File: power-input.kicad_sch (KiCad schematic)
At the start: 21 parts, among them J204 Conn_01x02, J301 Conn_01x02, U202 XL1509-3.3

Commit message: Rename Ferrite_Bead to FerriteBead
Symbol name changed between KiCad 5 and 6...
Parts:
- FB301: symbol Device:Ferrite_Bead -> Device:FerriteBead
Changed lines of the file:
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@@
     (pin "2")
   )
-  (symbol (lib_id "Device:Ferrite_Bead") (at 113.03 53.34 270) (unit 1)
+  (symbol (lib_id "Device:FerriteBead") (at 113.03 53.34 270) (unit 1)
     (in_bom yes) (on_board yes)
     (property "Reference" "FB301" (id 0) (at 113.03 46.3804 90))

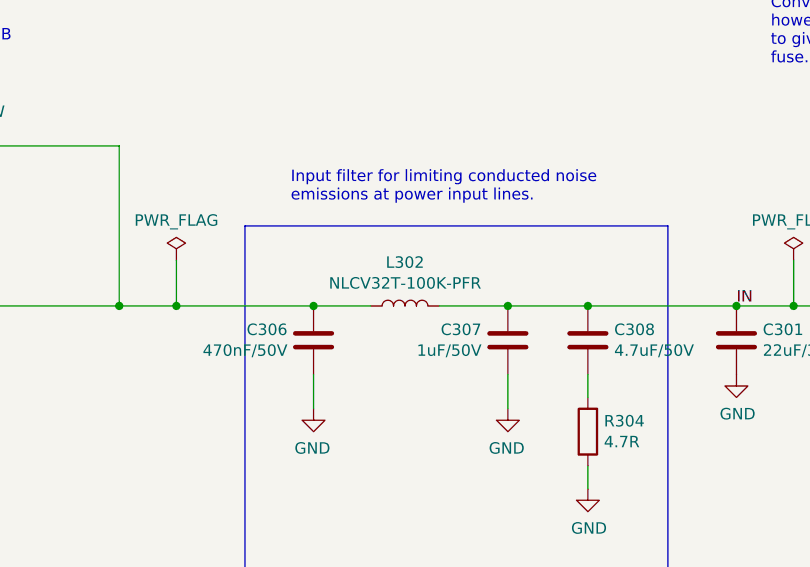
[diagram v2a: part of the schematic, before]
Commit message: One more component swap due to part availability
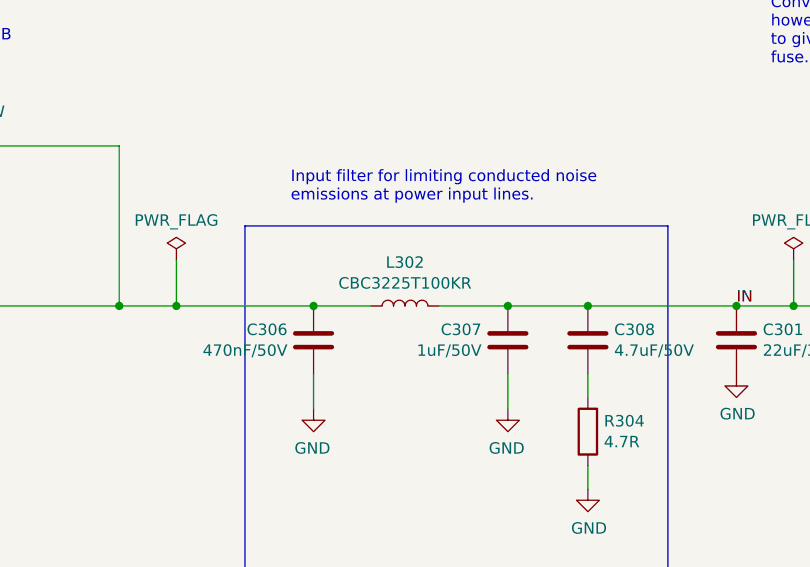
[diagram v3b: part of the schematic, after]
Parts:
- L302: value NLCV32T-100K-PFR -> CBC3225T100KR; LCSC C74563 -> C90321; Notes Alternative: CBC3225T100KR -> Alternatives: CBC3225T100KR, NLCV32T-100K-PFR
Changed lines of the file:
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@@
     (in_bom yes) (on_board yes)
     (property "Reference" "L302" (id 0) (at 121.92 117.094 90))
-    (property "Value" "NLCV32T-100K-PFR" (id 1) (at 121.92 119.4054 90))
+    (property "Value" "CBC3225T100KR" (id 1) (at 121.92 119.4054 90))
     (property "Footprint" "Inductor_SMD:L_1210_3225Metric" (id 2) (at 121.92 121.92 0)
       (effects (font (size 1.27 1.27)) hide)
@@
       (effects (font (size 1.27 1.27)) hide)
     )
-    (property "LCSC" "C74563" (id 6) (at 121.92 121.92 0)
+    (property "LCSC" "C90321" (id 6) (at 121.92 121.92 0)
       (effects (font (size 1.27 1.27)) hide)
     )
-    (property "Notes" "Alternative: CBC3225T100KR" (id 7) (at 121.92 121.92 90)
+    (property "Notes" "Alternatives: CBC3225T100KR, NLCV32T-100K-PFR" (id 7) (at 121.92 121.92 90)
       (effects (font (size 1.27 1.27)) hide)
     )

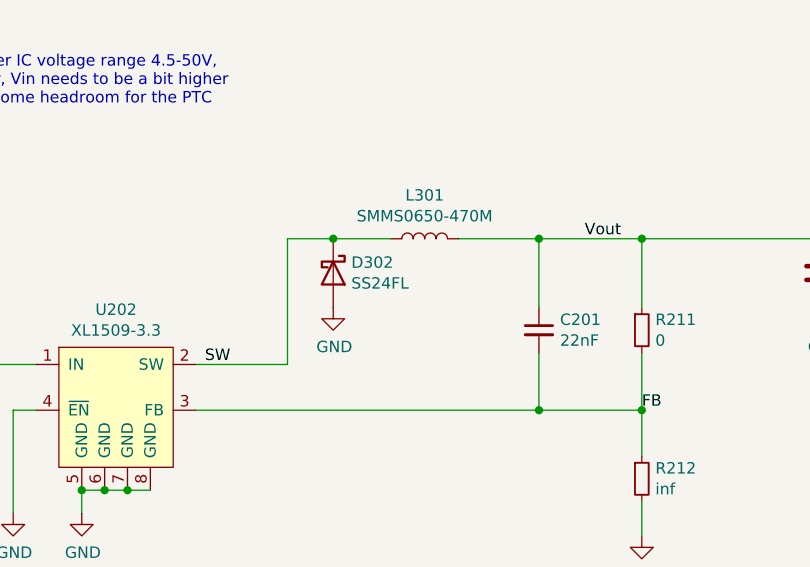
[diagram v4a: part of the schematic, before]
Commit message: Change parts according to JLCPCB availability
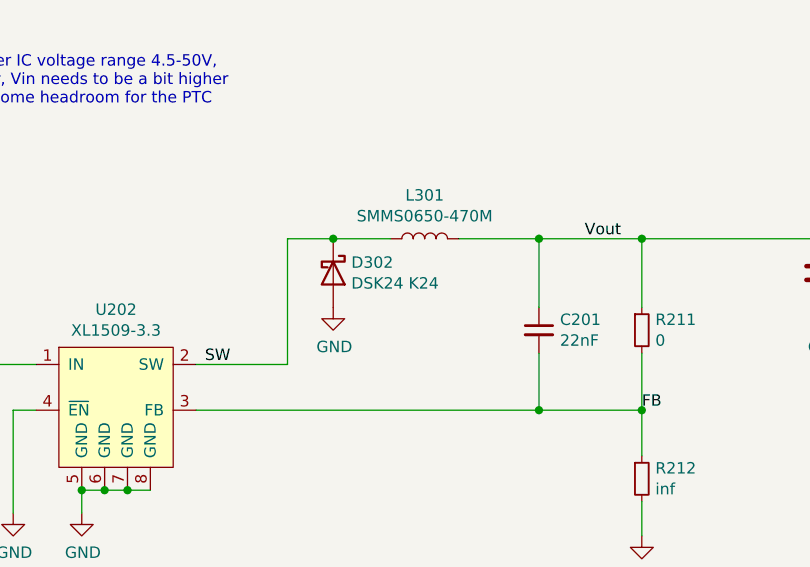
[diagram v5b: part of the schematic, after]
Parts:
- C301: LCSC C342620 -> C778721
- D302: value SS24FL -> DSK24 K24; LCSC C489144 -> C64890
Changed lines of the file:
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@@
       (effects (font (size 1.27 1.27)) hide)
     )
-    (property "LCSC" "C342620" (id 5) (at 158.75 125.73 0)
+    (property "LCSC" "C778721" (id 5) (at 158.75 125.73 0)
       (effects (font (size 1.27 1.27)) hide)
     )
@@
       (effects (font (size 1.27 1.27)) (justify left))
     )
-    (property "Value" "SS24FL" (id 1) (at 209.0166 112.903 90)
+    (property "Value" "DSK24 K24" (id 1) (at 209.0166 112.903 90)
       (effects (font (size 1.27 1.27)) (justify left))
     )
@@
       (effects (font (size 1.27 1.27)) hide)
     )
-    (property "LCSC" "C489144" (id 5) (at 207.01 111.76 0)
+    (property "LCSC" "C64890" (id 5) (at 207.01 111.76 0)
       (effects (font (size 1.27 1.27)) hide)
     )

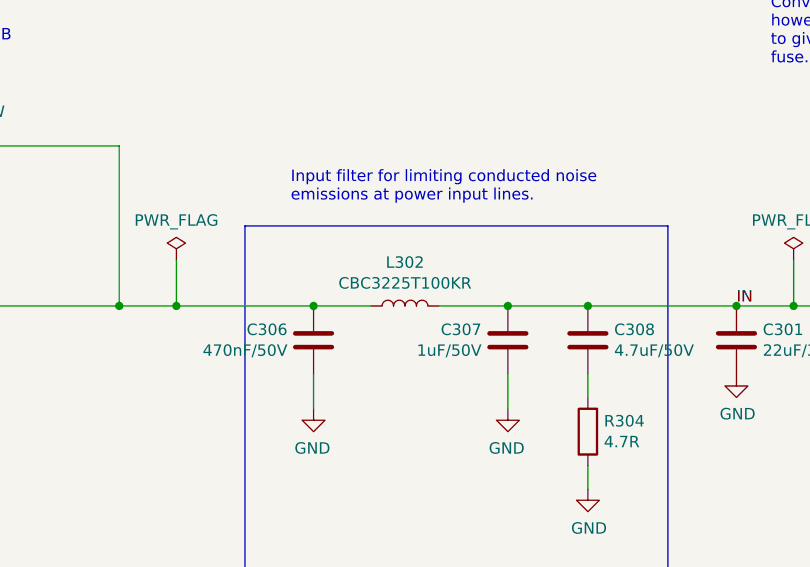
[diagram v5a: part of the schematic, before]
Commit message: Change the filter inductor according to JLC availability
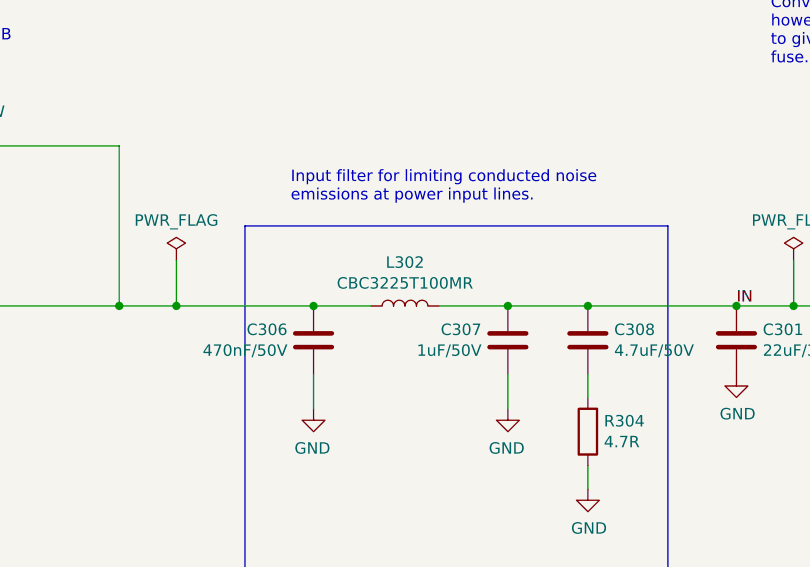
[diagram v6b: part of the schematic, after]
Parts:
- L302: value CBC3225T100KR -> CBC3225T100MR; LCSC C90321 -> C90315
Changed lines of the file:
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@@
     (in_bom yes) (on_board yes)
     (property "Reference" "L302" (id 0) (at 121.92 117.094 90))
-    (property "Value" "CBC3225T100KR" (id 1) (at 121.92 119.4054 90))
+    (property "Value" "CBC3225T100MR" (id 1) (at 121.92 119.4054 90))
     (property "Footprint" "Inductor_SMD:L_1210_3225Metric" (id 2) (at 121.92 121.92 0)
       (effects (font (size 1.27 1.27)) hide)
@@
       (effects (font (size 1.27 1.27)) hide)
     )
-    (property "LCSC" "C90321" (id 6) (at 121.92 121.92 0)
+    (property "LCSC" "C90315" (id 6) (at 121.92 121.92 0)
       (effects (font (size 1.27 1.27)) hide)
     )

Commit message: Fix component rotations
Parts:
- J301: JLCPCB_CORRECTION (none) -> 1.905;0;180
- U202: JLCPCB_CORRECTION (none) -> 0;0;270
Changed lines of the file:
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@@
       (effects (font (size 1.27 1.27)) hide)
     )
-    (property "JLCPCB_CORRECTION" "" (at 44.45 50.8 0)
+    (property "JLCPCB_CORRECTION" "1.905;0;180" (at 44.45 50.8 0)
       (effects (font (size 1.27 1.27)) hide)
     )
@@
       (effects (font (size 1.27 1.27)) hide)
     )
-    (property "JLCPCB_CORRECTION" "" (at 182.88 127 0)
-      (effects (font (size 1.27 1.27)) hide)
-    )
+    (property "JLCPCB_CORRECTION" "0;0;270" (at 182.88 127 0)
+      (effects (font (size 1.27 1.27)) hide)
+    )
